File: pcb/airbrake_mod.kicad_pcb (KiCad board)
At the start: 4 copper layers, 65.7 x 107.9 mm, 142 parts, among them J1 XT30PW-M, J2 Same Sky UJ20-C-H-G-SMT-P16-TR, J3 0436500415, J6 CNC_Tech_3220-14-0100-00, Q1 NTR4003N, Q2 NTR4003N, Q3 Si3407DV, Q4 NTR4003N, Q5 Si3407DV, Q6 NTR4003N, SW1 GSPTS0018, SW2 GSPTS0018, SW4 GSPTS0018, SW5 GSPTS0018, SW6 GSPTS0018, SW7 GSPTS0018, U1 STM32H730VBTx, U2 TPS561246DRLR, U3 ZXCT180A4W5, U4 USBLC6-2SC6, U5 W25Q128JVS, U6 LPS22DF, U7 LSM6DSV80X, U8 IIS2MDC, Y1 ECS-160-12-33B2Q-JES-TR3

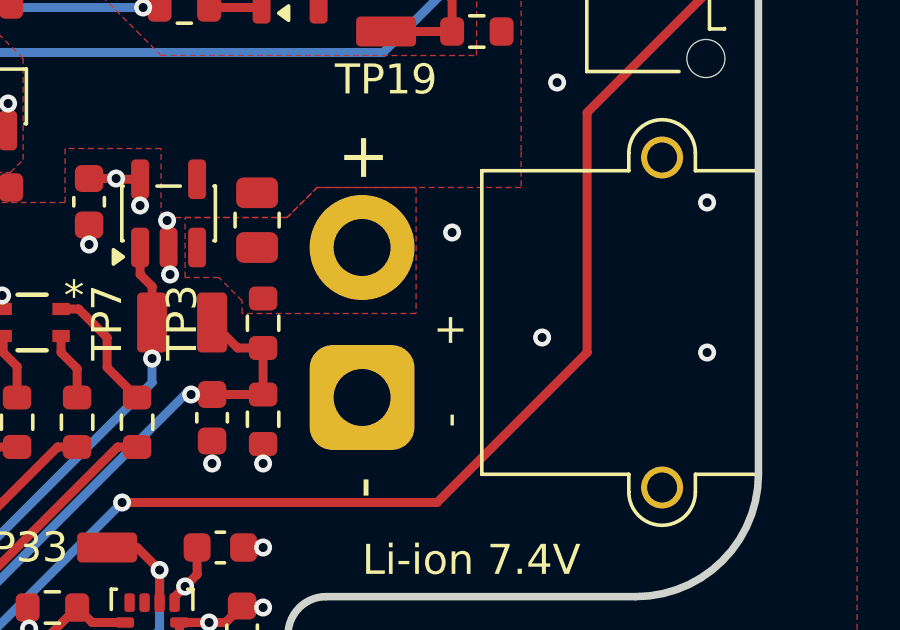
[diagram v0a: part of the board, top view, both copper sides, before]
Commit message: Remove extra silkscreen text
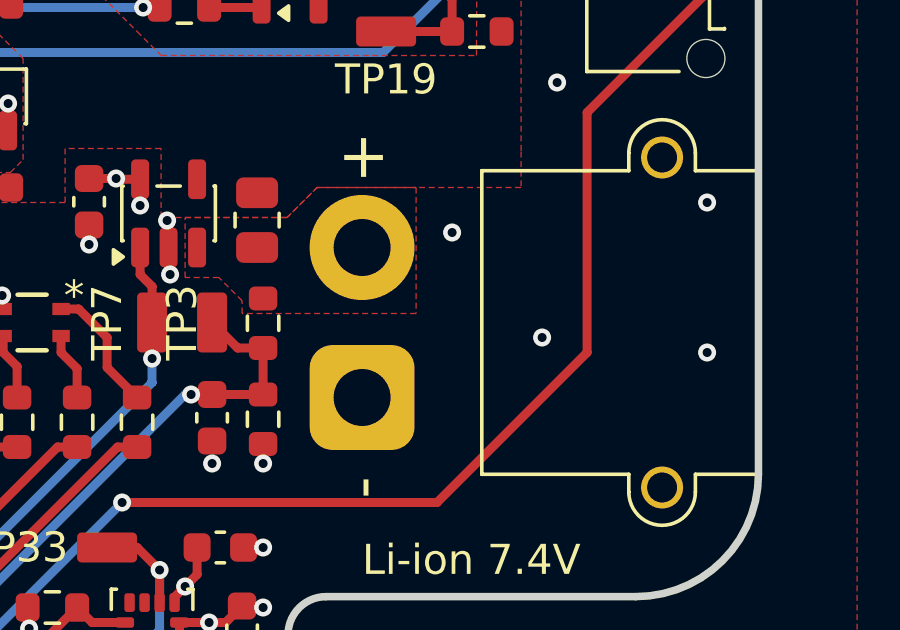
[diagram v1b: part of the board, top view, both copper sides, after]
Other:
- board text removed: "- +"
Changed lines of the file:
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@@
 		(layer "Edge.Cuts")
-	)
-	(gr_text "-     +"
-		(at 102 77.5 90)
-		(layer "F.SilkS")
-		(effects
-			(font
-				(size 1 1)
-				(thickness 0.15)
-			)
-			(justify left bottom)
-		)
 	)
 	(gr_text "SERVO"

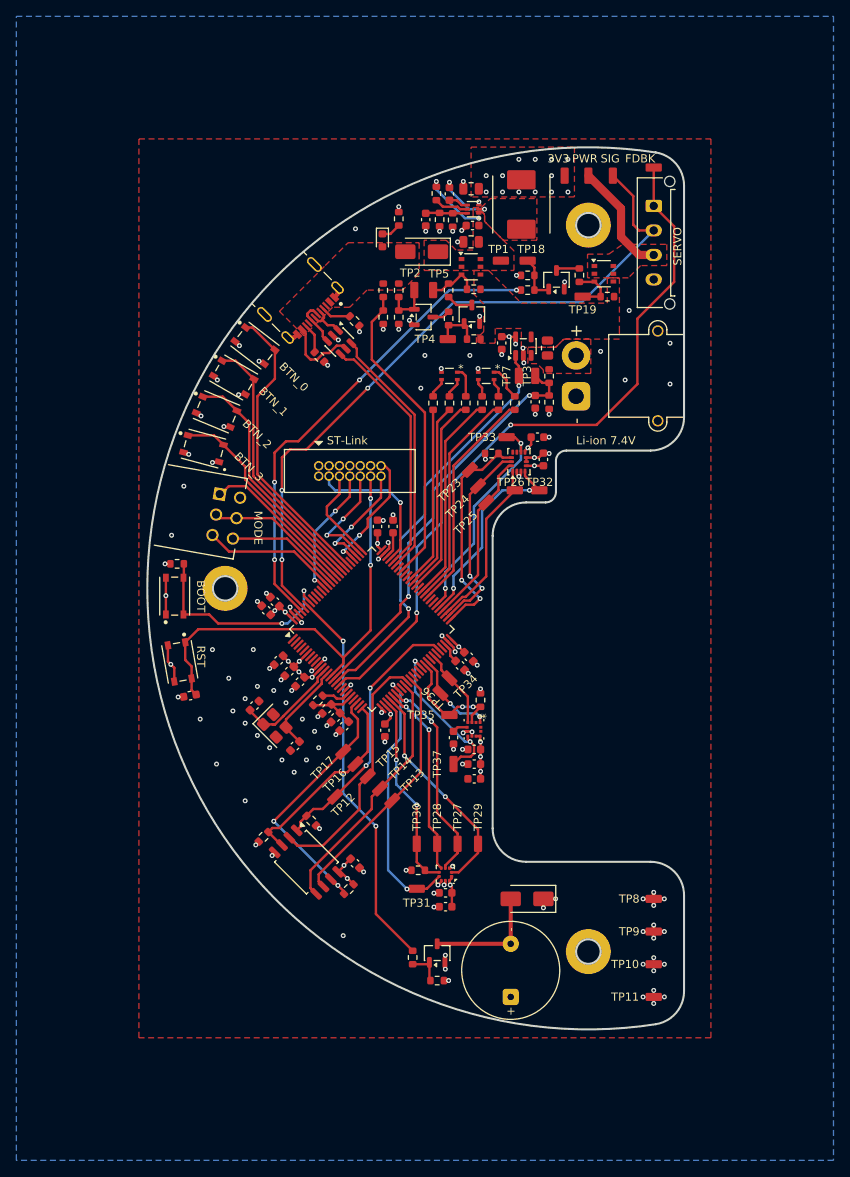
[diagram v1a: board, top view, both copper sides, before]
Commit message: Add buck enable switch
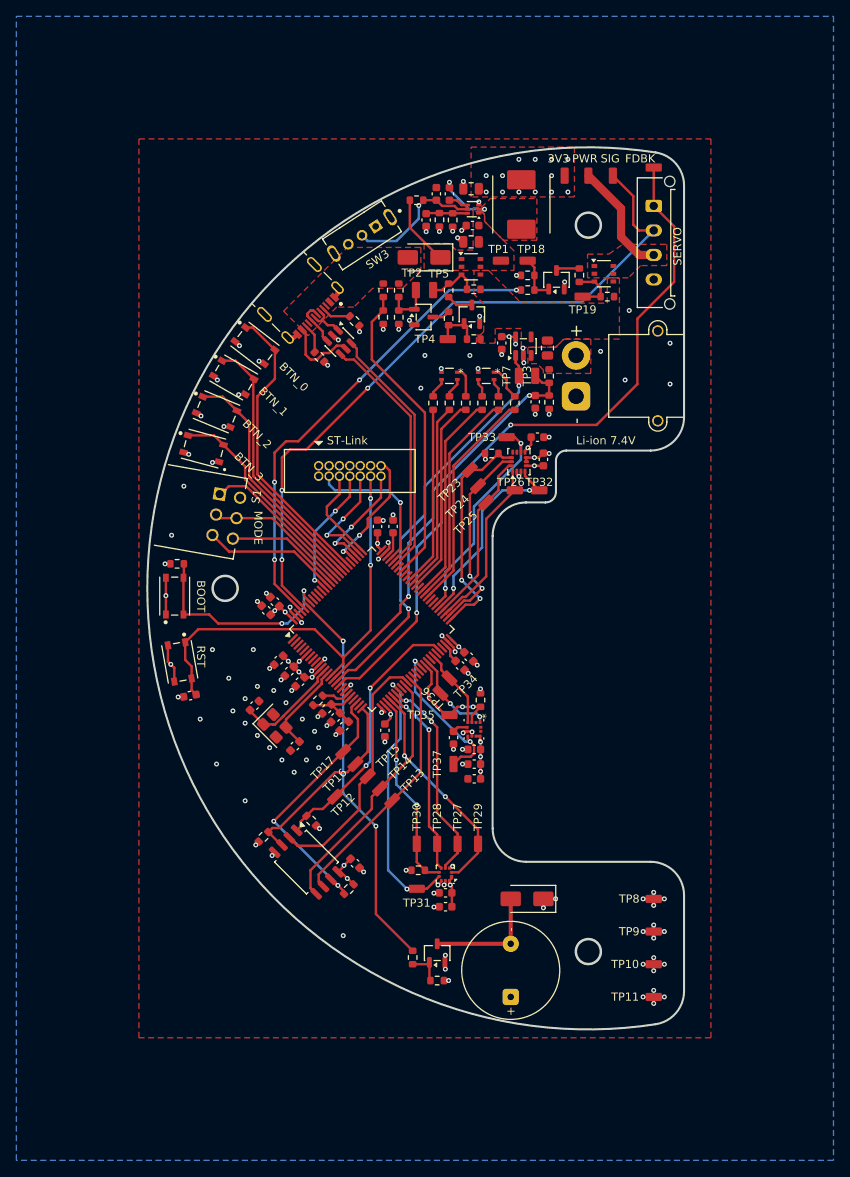
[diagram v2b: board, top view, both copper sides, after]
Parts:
- removed D2: B1911USD, LED_SMD:LED_0603_1608Metric
- removed R19: 600, Resistor_SMD:R_0603_1608Metric
- added C18: 1u, Capacitor_SMD:C_0603_1608Metric, F.Cu at (81.4, 51.7)
- added SW3: SLW-864574-5A-RA-N-D, SW_SameSky:SW_SameSky_SLW-864574-5A-RA-N-D, F.Cu at (72.3, 56.8)
- S1: footprint SW_SameSky_RDS4-8S-1012-73-RA-254-D-67:SW_RDS4-8S-1012-73-RA-254-D-67 -> SW_SameSky:SW_SameSky_RDS4-8S-1012-73-RA-254-D-67
- moved R6 2.56 mm to (79.0, 52.5), turned to 0 degrees
- moved D1 0.76 mm to (79.9, 59.5)
- moved TP2 0.20 mm to (78.9, 63.5)
- moved C21 0.07 mm to (80.2, 54.9)
- renumbered C18 to C19, C19 to C20, C20 to C21, C21 to C22, C22 to C23, C23 to C24, C24 to C25, C25 to C26, C26 to C27, C27 to C28, C28 to C29, C29 to C30, C30 to C31, C31 to C32
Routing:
- net Net-(SW3-B): track 4.23 -> 16.7 mm, vias 0 -> 1
- net Net-(D2-K): track 2.42 -> 0.00 mm
- net /Power/BUCK_IN: track 8.30 -> 9.11 mm, vias 2 -> 0
- net GND: track 55.7 -> 55.3 mm, vias 104 -> 102

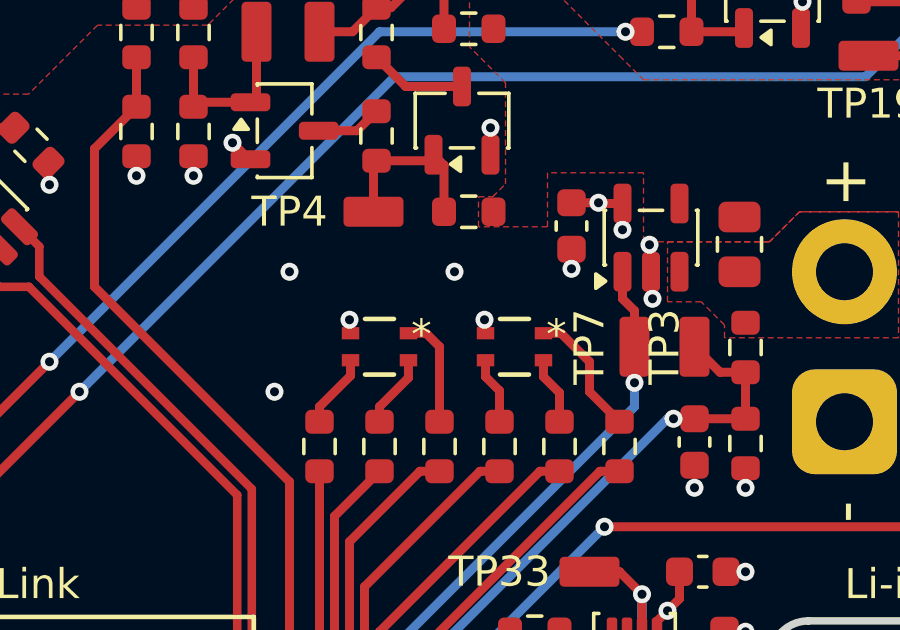
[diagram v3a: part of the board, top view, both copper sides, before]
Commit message: Add 3D models for B38G3RGB
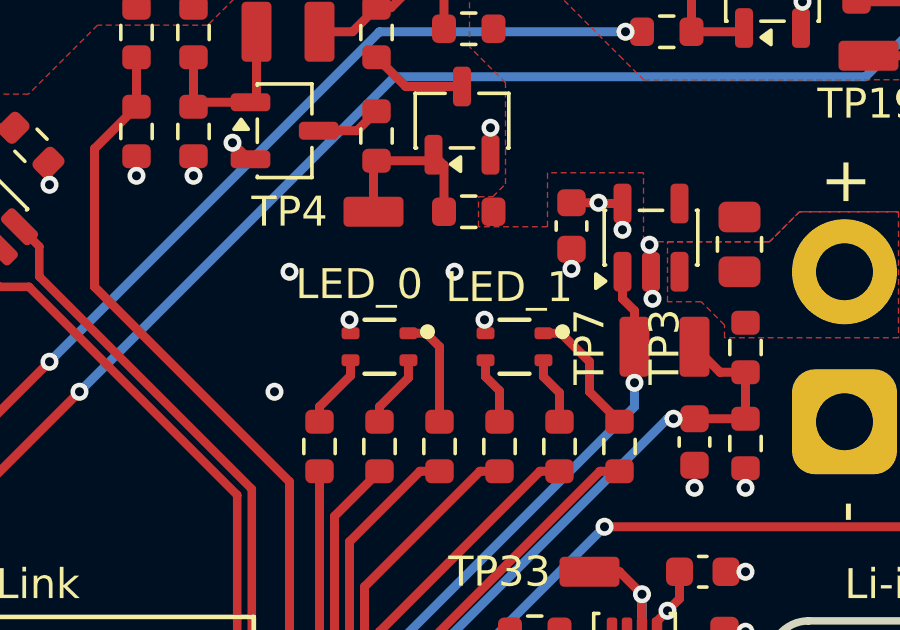
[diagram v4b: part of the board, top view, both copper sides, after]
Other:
- board text added: "LED_0"
- board text added: "LED_1"

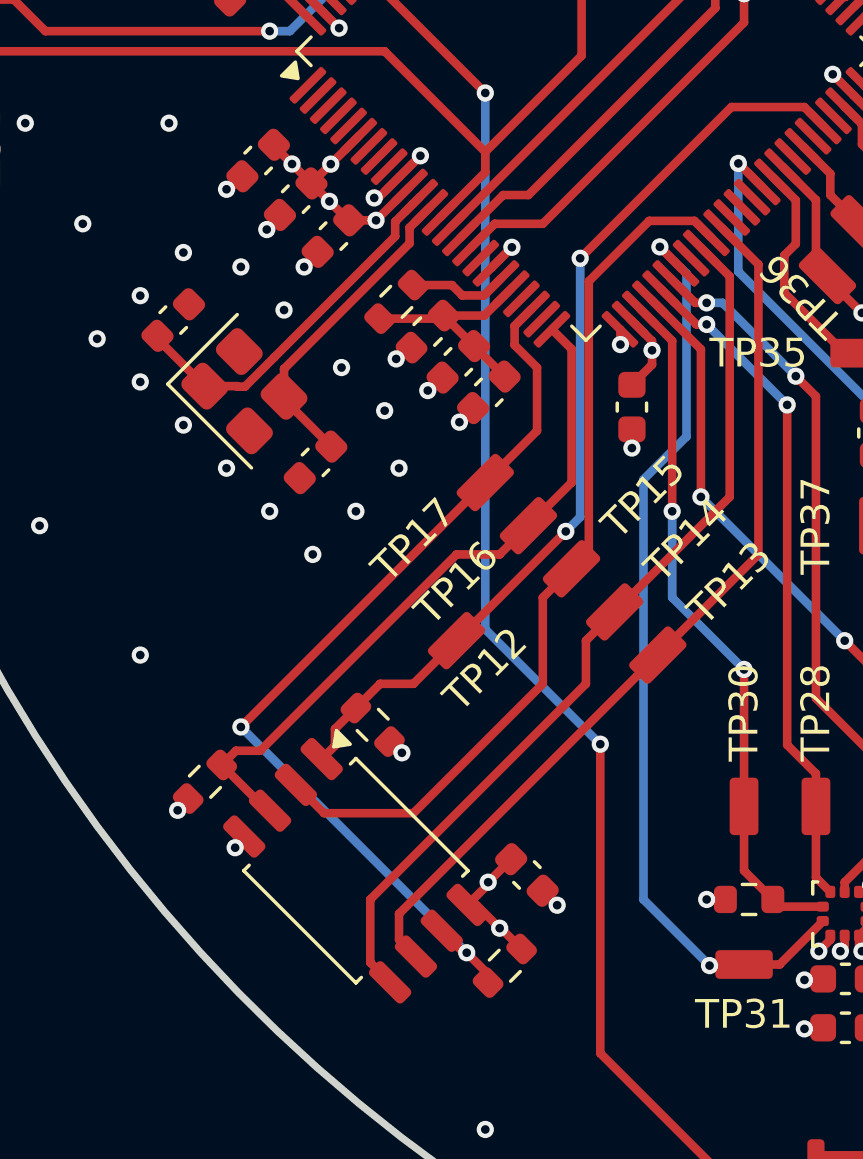
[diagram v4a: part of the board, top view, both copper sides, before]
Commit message: Tune high speed routing
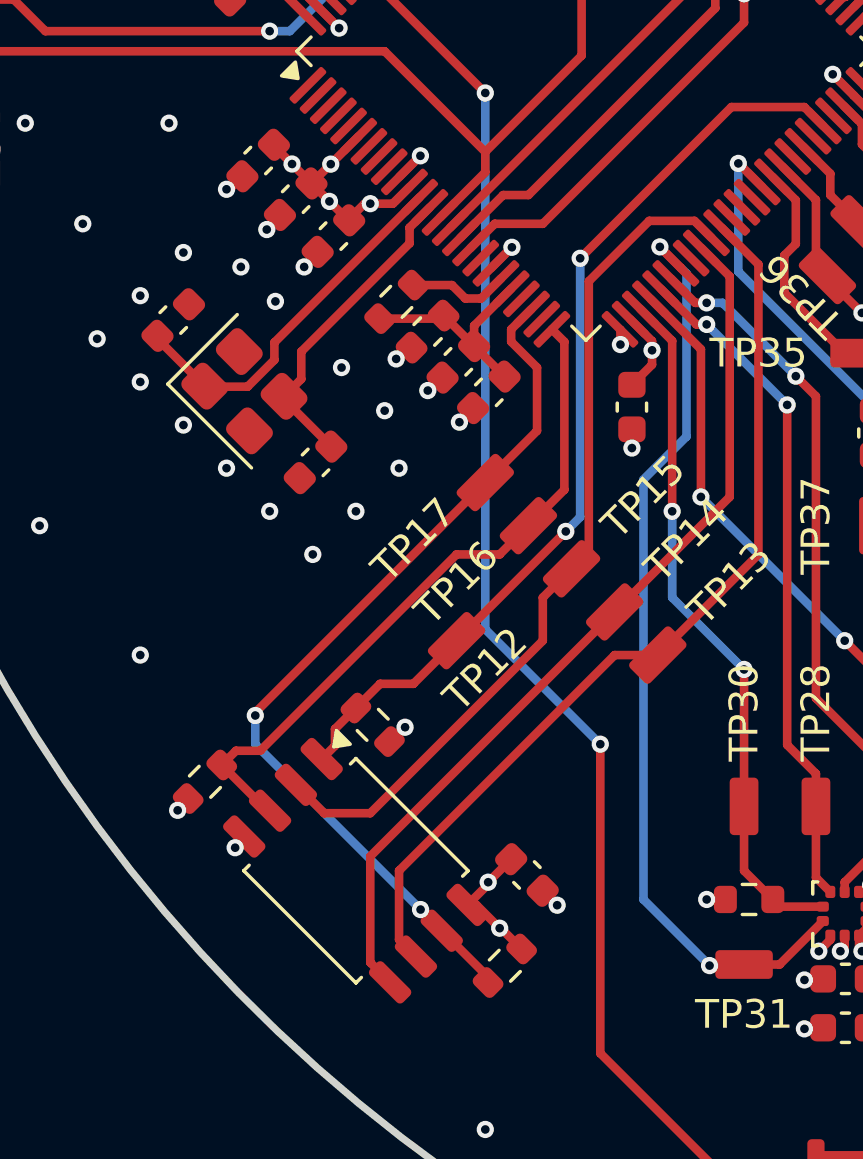
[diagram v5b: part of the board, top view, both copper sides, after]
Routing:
- net /Flash/IO3: track 33.0 -> 31.5 mm
- net GND: track 55.3 -> 54.1 mm, vias 102 -> 101
- net /Flash/IO1: track 30.9 -> 30.0 mm
- net /Flash/CLK: track 31.3 -> 32.2 mm
